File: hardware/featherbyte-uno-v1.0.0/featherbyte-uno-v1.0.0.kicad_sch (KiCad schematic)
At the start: 60 parts, among them J1 Conn_01x08, J10 Conn_01x09, J2 Conn_01x10, J3 Conn_01x06, J5 USB_C_Receptacle_16P, J6 SWD Connector, J7 Terminal Block, J8 USB_C_Receptacle_16P, J9 BOOT1, SW1 Reset, SW2 BOOT0, SW3 SW_DIP_x04, U1 CH32V203CxT6, U2 TJA1050, U4 AMS1117-3.3, U5 USBLC6-2P6, U6 USBLC6-2P6, Y1 8M, Y3 32.768K

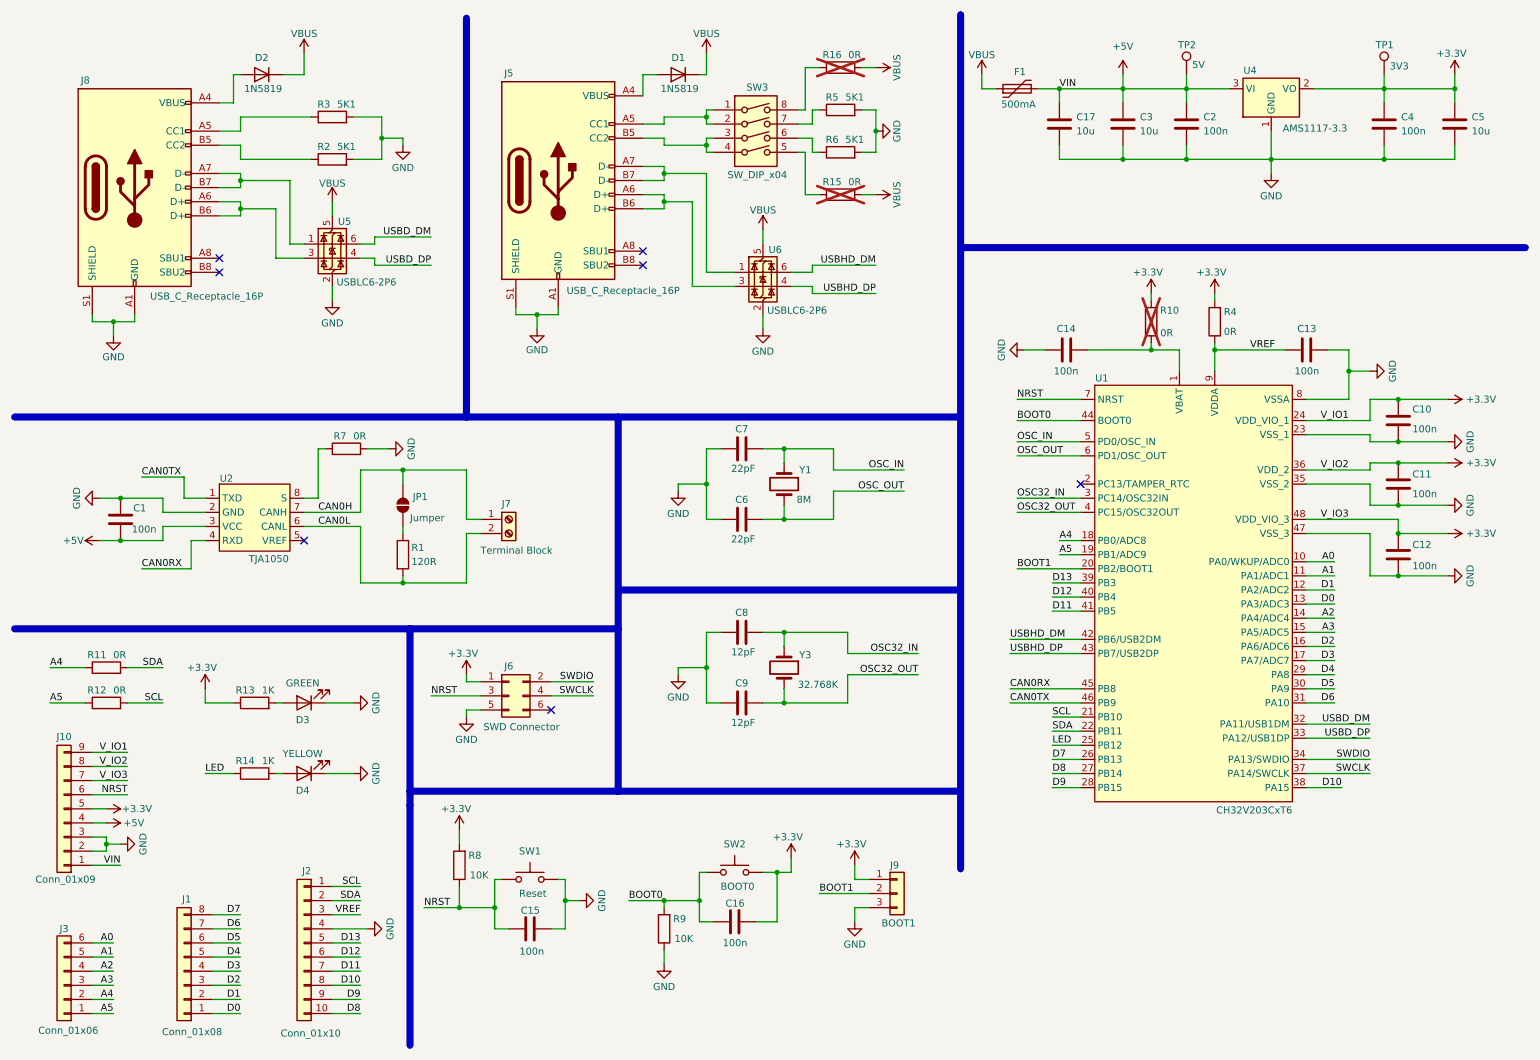
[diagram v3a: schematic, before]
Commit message: usb tvs diode orientation changed
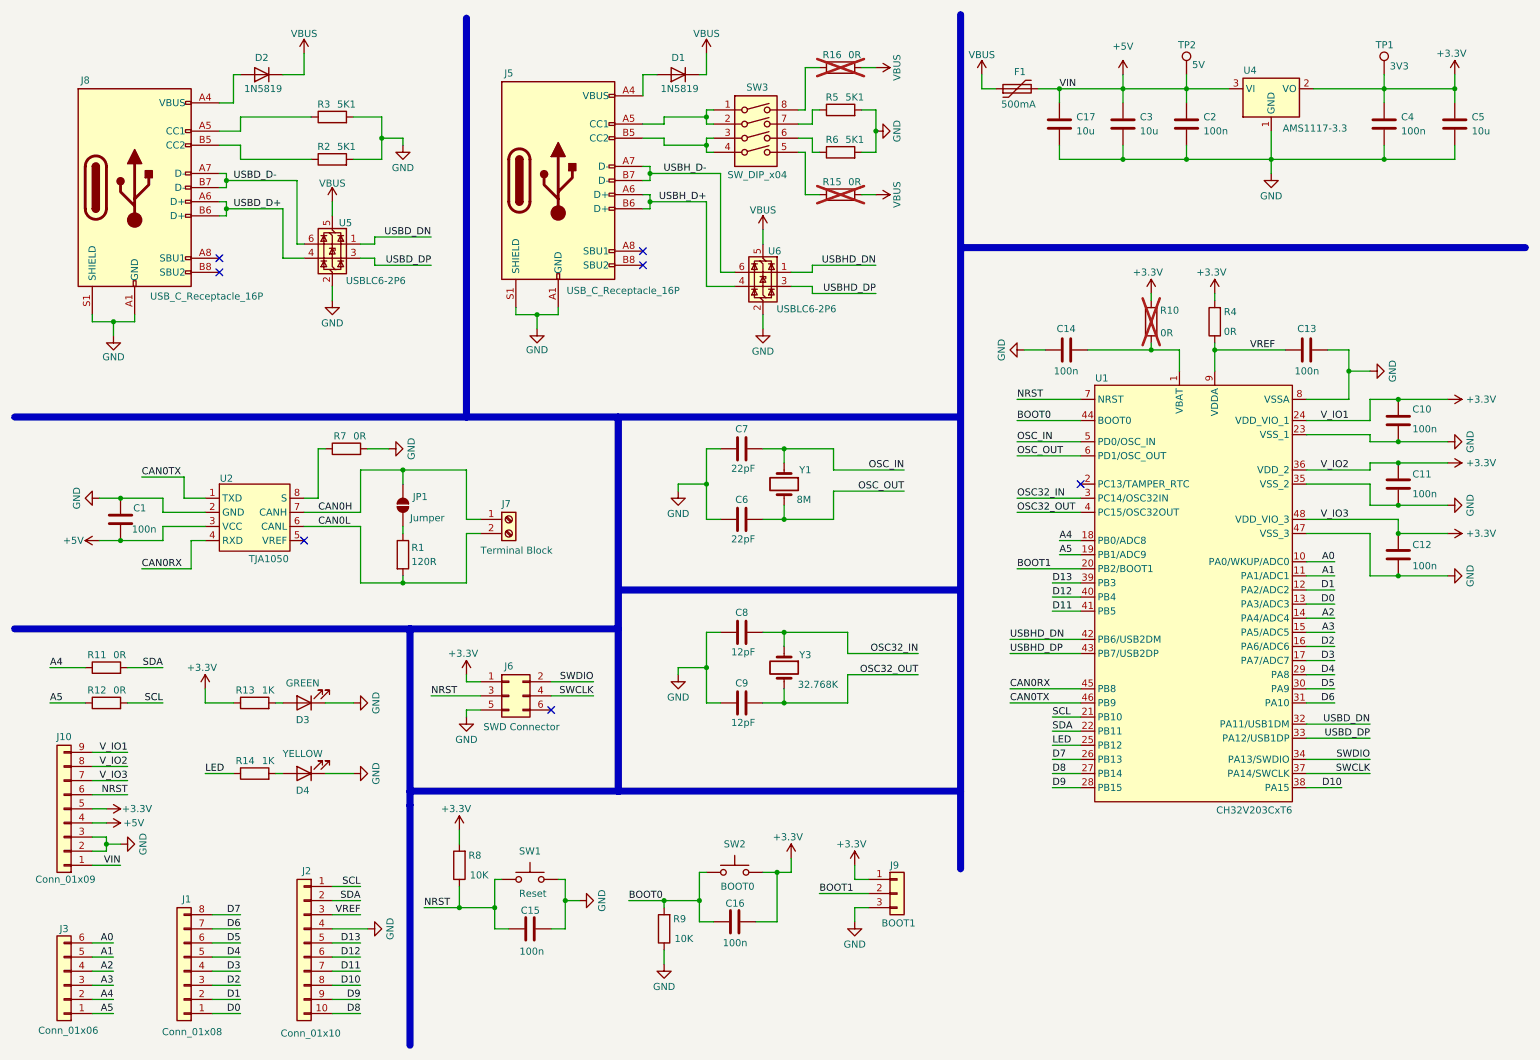
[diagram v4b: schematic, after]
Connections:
- net USBD_DP: now also U5.3 (I/O2); no longer U5.4 (I/O2)
- net USBHD_DP: now also U6.3 (I/O2); no longer U6.4 (I/O2)
- net USBD_D-: now reaches J8.A7 (D-), J8.B7 (D-)
- net USBD_D-: now also U5.6 (I/O1); no longer U5.1 (I/O1)
- net USBD_D+: now reaches J8.A6 (D+), J8.B6 (D+)
- net USBD_D+: now also U5.4 (I/O2); no longer U5.3 (I/O2)
- net USBH_D+: now reaches J5.A6 (D+), J5.B6 (D+)
- net USBH_D+: now also U6.4 (I/O2); no longer U6.3 (I/O2)
- net USBH_D-: now reaches J5.A7 (D-), J5.B7 (D-)
- net USBH_D-: now also U6.6 (I/O1); no longer U6.1 (I/O1)
- net USBD_DM renamed USBD_DN
- net USBD_DN: now also U5.1 (I/O1); no longer U5.6 (I/O1)
- net USBHD_DM renamed USBHD_DN
- net USBHD_DN: now also U6.1 (I/O1); no longer U6.6 (I/O1)

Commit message: can bus connector pins reversed
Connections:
- net CAN0H: now also J7.2 (Pin_2); no longer J7.1 (Pin_1)
- net CAN0L: now also J7.1 (Pin_1); no longer J7.2 (Pin_2)
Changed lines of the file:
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@@
 	(wire
 		(pts
+			(xy 93.98 105.41) (xy 96.52 105.41)
+		)
+		(stroke
+			(width 0)
+			(type default)
+		)
+	)
+	(wire
+		(pts
 			(xy 127 41.91) (xy 125.73 41.91)
 		)
@@
 	(wire
 		(pts
-			(xy 93.98 105.41) (xy 96.52 105.41)
-		)
-		(stroke
-			(width 0)
-			(type default)
-		)
-	)
-	(wire
-		(pts
 			(xy 162.56 135.89) (xy 162.56 130.81)
 		)
@@
 	(wire
 		(pts
-			(xy 93.98 102.87) (xy 96.52 102.87)
-		)
-		(stroke
-			(width 0)
-			(type default)
-		)
-	)
-	(wire
-		(pts
 			(xy 77.47 52.07) (xy 77.47 53.34)
 		)
@@
 	(wire
 		(pts
+			(xy 93.98 102.87) (xy 96.52 102.87)
+		)
+		(stroke
+			(width 0)
+			(type default)
+		)
+	)
+	(wire
+		(pts
 			(xy 129.54 35.56) (xy 129.54 34.29)
 		)
@@
 	(symbol
 		(lib_id "Connector:Screw_Terminal_01x02")
-		(at 101.6 102.87 0)
+		(at 101.6 105.41 0)
+		(mirror x)
 		(unit 1)
 		(exclude_from_sim no)
@@
 		(dnp no)
 		(property "Reference" "J7"
-			(at 100.33 100.076 0)
+			(at 100.838 100.584 0)
 			(effects
 				(font
@@
 		)
 		(property "Value" "Terminal Block"
-			(at 96.52 108.458 0)
+			(at 96.52 108.204 0)
 			(effects
 				(font
@@
 		)
 		(property "Footprint" "TerminalBlock:TerminalBlock_MaiXu_MX126-5.0-02P_1x02_P5.00mm"
-			(at 101.6 102.87 0)
+			(at 101.6 105.41 0)
 			(effects
 				(font
@@
 		)
 		(property "Datasheet" "~"
-			(at 101.6 102.87 0)
+			(at 101.6 105.41 0)
 			(effects
 				(font
@@
 		)
 		(property "Description" "Generic screw terminal, single row, 01x02, script generated (kicad-library-utils/schlib/autogen/connector/)"
-			(at 101.6 102.87 0)
+			(at 101.6 105.41 0)
 			(effects
 				(font

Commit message: pcb routing ongoing
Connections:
- net USBD_D+: now also U5.3 (I/O2); no longer U5.4 (I/O2)
- net USBD_D-: now also U5.1 (I/O1); no longer U5.6 (I/O1)
- net USBD_DN: now also U5.6 (I/O1); no longer U5.1 (I/O1)
- net USBD_DP: now also U5.4 (I/O2); no longer U5.3 (I/O2)
- net USBHD_DN: now also U6.6 (I/O1); no longer U6.1 (I/O1)
- net USBHD_DP: now also U6.4 (I/O2); no longer U6.3 (I/O2)
- net USBH_D+: now also U6.3 (I/O2); no longer U6.4 (I/O2)
- net USBH_D-: now also U6.1 (I/O1); no longer U6.6 (I/O1)
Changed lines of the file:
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@@
 	(wire
 		(pts
+			(xy 137.16 60.96) (xy 142.24 60.96)
+		)
+		(stroke
+			(width 0)
+			(type default)
+		)
+	)
+	(wire
+		(pts
 			(xy 245.11 85.09) (xy 256.54 85.09)
 		)
@@
 	(wire
 		(pts
+			(xy 139.7 58.42) (xy 142.24 58.42)
+		)
+		(stroke
+			(width 0)
+			(type default)
+		)
+	)
+	(wire
+		(pts
 			(xy 223.52 25.4) (xy 231.14 25.4)
 		)
@@
 	(wire
 		(pts
-			(xy 137.16 60.96) (xy 142.24 60.96)
-		)
-		(stroke
-			(width 0)
-			(type default)
-		)
-	)
-	(wire
-		(pts
 			(xy 250.19 133.35) (xy 245.11 133.35)
 		)
@@
 	(wire
 		(pts
-			(xy 152.4 60.96) (xy 156.21 60.96)
-		)
-		(stroke
-			(width 0)
-			(type default)
-		)
-	)
-	(wire
-		(pts
 			(xy 137.16 29.21) (xy 137.16 30.48)
 		)
@@
 	(wire
 		(pts
-			(xy 139.7 58.42) (xy 142.24 58.42)
-		)
-		(stroke
-			(width 0)
-			(type default)
-		)
-	)
-	(wire
-		(pts
 			(xy 250.19 128.27) (xy 245.11 128.27)
 		)
@@
 	(wire
 		(pts
+			(xy 74.93 55.88) (xy 77.47 55.88)
+		)
+		(stroke
+			(width 0)
+			(type default)
+		)
+	)
+	(wire
+		(pts
 			(xy 67.31 90.17) (xy 68.58 90.17)
 		)
@@
 	(wire
 		(pts
-			(xy 74.93 55.88) (xy 77.47 55.88)
-		)
-		(stroke
-			(width 0)
-			(type default)
-		)
-	)
-	(wire
-		(pts
 			(xy 26.67 162.56) (xy 29.21 162.56)
 		)
@@
 	(wire
 		(pts
-			(xy 74.93 114.3) (xy 82.55 114.3)
+			(xy 63.5 53.34) (xy 64.77 53.34)
 		)
 		(stroke
@@
 	(wire
 		(pts
-			(xy 152.4 58.42) (xy 156.21 58.42)
+			(xy 74.93 114.3) (xy 82.55 114.3)
 		)
 		(stroke
@@
 	(wire
 		(pts
-			(xy 60.96 55.88) (xy 64.77 55.88)
+			(xy 162.56 123.19) (xy 151.13 123.19)
 		)
 		(stroke
@@
 	(wire
 		(pts
-			(xy 162.56 123.19) (xy 151.13 123.19)
+			(xy 137.16 90.17) (xy 137.16 96.52)
 		)
 		(stroke
@@
 	(wire
 		(pts
-			(xy 137.16 90.17) (xy 137.16 96.52)
+			(xy 78.74 34.29) (xy 78.74 38.1)
 		)
 		(stroke
@@
 	(wire
 		(pts
-			(xy 78.74 34.29) (xy 78.74 38.1)
+			(xy 64.77 101.6) (xy 74.93 101.6)
 		)
 		(stroke
@@
 	(wire
 		(pts
-			(xy 64.77 101.6) (xy 74.93 101.6)
+			(xy 200.66 25.4) (xy 212.09 25.4)
 		)
 		(stroke
@@
 	(wire
 		(pts
-			(xy 200.66 25.4) (xy 212.09 25.4)
+			(xy 152.4 58.42) (xy 156.21 58.42)
 		)
 		(stroke
@@
 	(wire
 		(pts
+			(xy 60.96 55.88) (xy 64.77 55.88)
+		)
+		(stroke
+			(width 0)
+			(type default)
+		)
+	)
+	(wire
+		(pts
 			(xy 50.8 40.64) (xy 50.8 41.91)
 		)
@@
 	(wire
 		(pts
-			(xy 63.5 53.34) (xy 64.77 53.34)
-		)
-		(stroke
-			(width 0)
-			(type default)
-		)
-	)
-	(wire
-		(pts
 			(xy 250.19 125.73) (xy 245.11 125.73)
 		)
@@
 	(wire
 		(pts
+			(xy 74.93 53.34) (xy 77.47 53.34)
+		)
+		(stroke
+			(width 0)
+			(type default)
+		)
+	)
+	(wire
+		(pts
 			(xy 186.69 25.4) (xy 189.23 25.4)
 		)
@@
 	(wire
 		(pts
-			(xy 74.93 53.34) (xy 77.47 53.34)
-		)
-		(stroke
-			(width 0)
-			(type default)
-		)
-	)
-	(wire
-		(pts
 			(xy 93.98 137.16) (xy 93.98 138.43)
 		)
@@
 	(wire
 		(pts
+			(xy 152.4 60.96) (xy 156.21 60.96)
+		)
+		(stroke
+			(width 0)
+			(type default)
+		)
+	)
+	(wire
+		(pts
 			(xy 46.99 133.35) (xy 46.99 135.89)
 		)
@@
 		(lib_id "Power_Protection:USBLC6-2P6")
 		(at 69.85 53.34 0)
-		(mirror y)
 		(unit 1)
 		(exclude_from_sim no)
@@
 		(dnp no)
 		(property "Reference" "U5"
-			(at 73.406 49.53 0)
+			(at 71.12 49.276 0)
 			(effects
 				(font
@@
 		)
 		(property "Value" "USBLC6-2P6"
-			(at 83.058 59.944 0)
+			(at 70.358 59.944 0)
 			(effects
 				(font
@@
 		)
 		(property "Footprint" "Package_TO_SOT_SMD:SOT-666"
-			(at 68.834 60.071 0)
+			(at 70.866 60.071 0)
 			(effects
 				(font
@@
 		)
 		(property "Datasheet" "https://www.st.com/resource/en/datasheet/usblc6-2.pdf"
-			(at 68.834 61.976 0)
+			(at 70.866 61.976 0)
 			(effects
 				(font
@@
 		(lib_id "Power_Protection:USBLC6-2P6")
 		(at 147.32 58.42 0)
-		(mirror y)
 		(unit 1)
 		(exclude_from_sim no)
@@
 		(dnp no)
 		(property "Reference" "U6"
-			(at 150.622 54.61 0)
+			(at 148.336 54.356 0)
 			(effects
 				(font
@@
 		)
 		(property "Value" "USBLC6-2P6"
-			(at 160.528 65.024 0)
+			(at 148.336 65.024 0)
 			(effects
 				(font
@@
 		)
 		(property "Footprint" "Package_TO_SOT_SMD:SOT-666"
-			(at 146.304 65.151 0)
+			(at 148.336 65.151 0)
 			(effects
 				(font
@@
 		)
 		(property "Datasheet" "https://www.st.com/resource/en/datasheet/usblc6-2.pdf"
-			(at 146.304 67.056 0)
+			(at 148.336 67.056 0)
 			(effects
 				(font

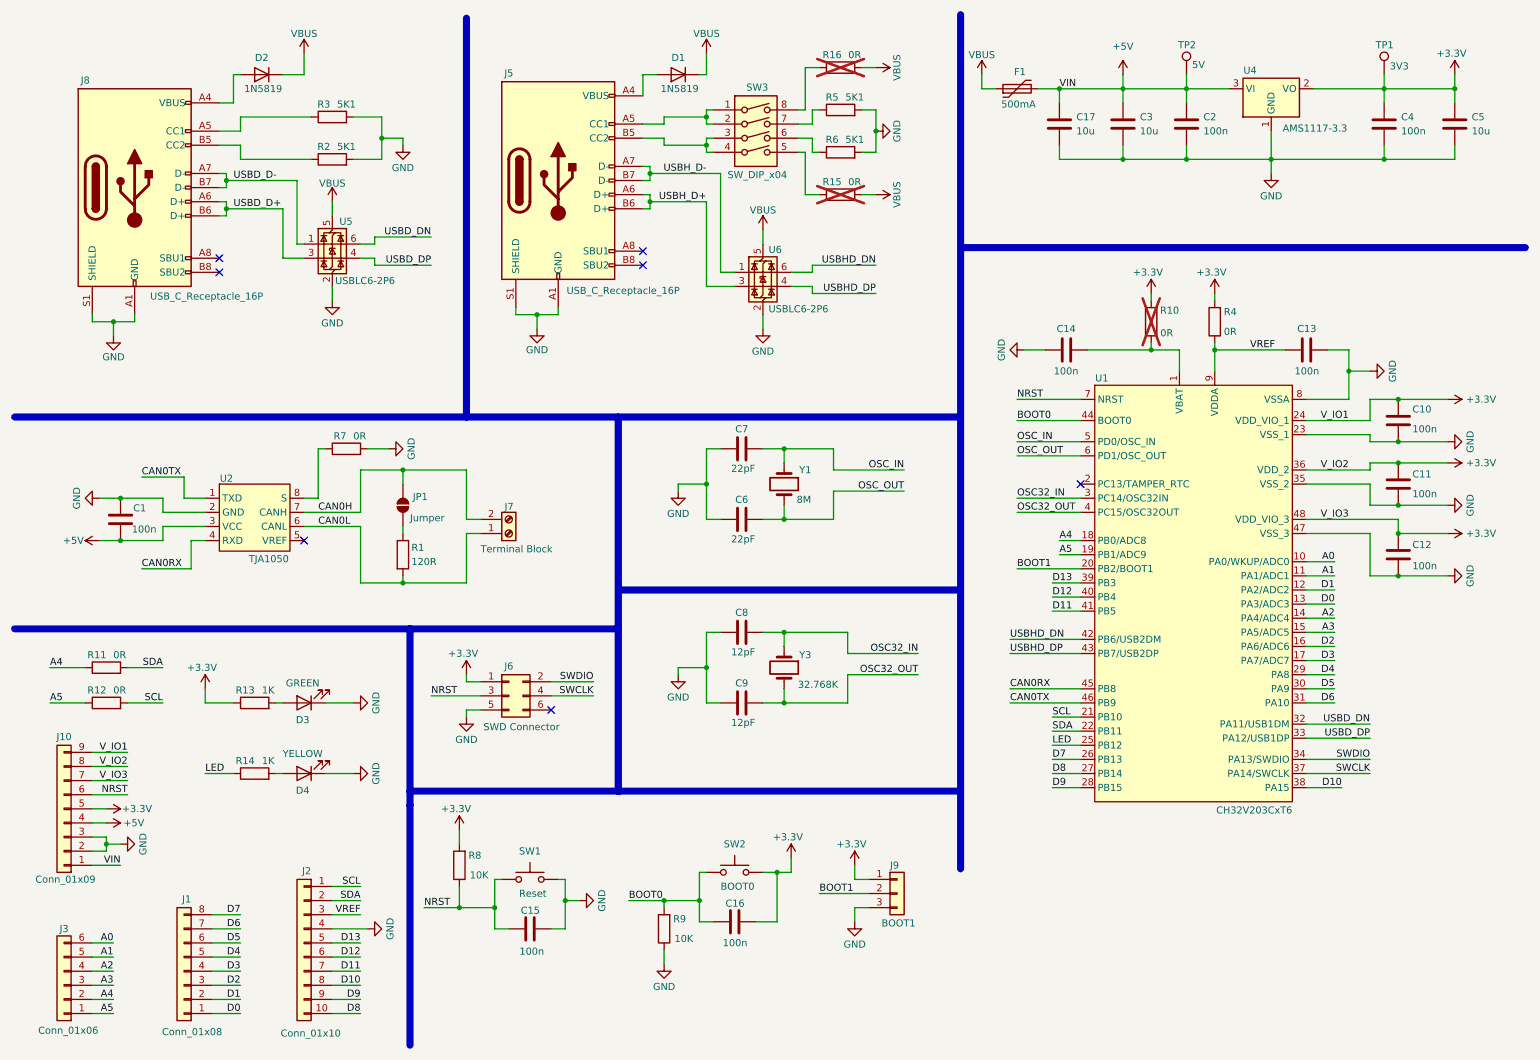
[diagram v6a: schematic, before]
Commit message: restarted routing and positioning process
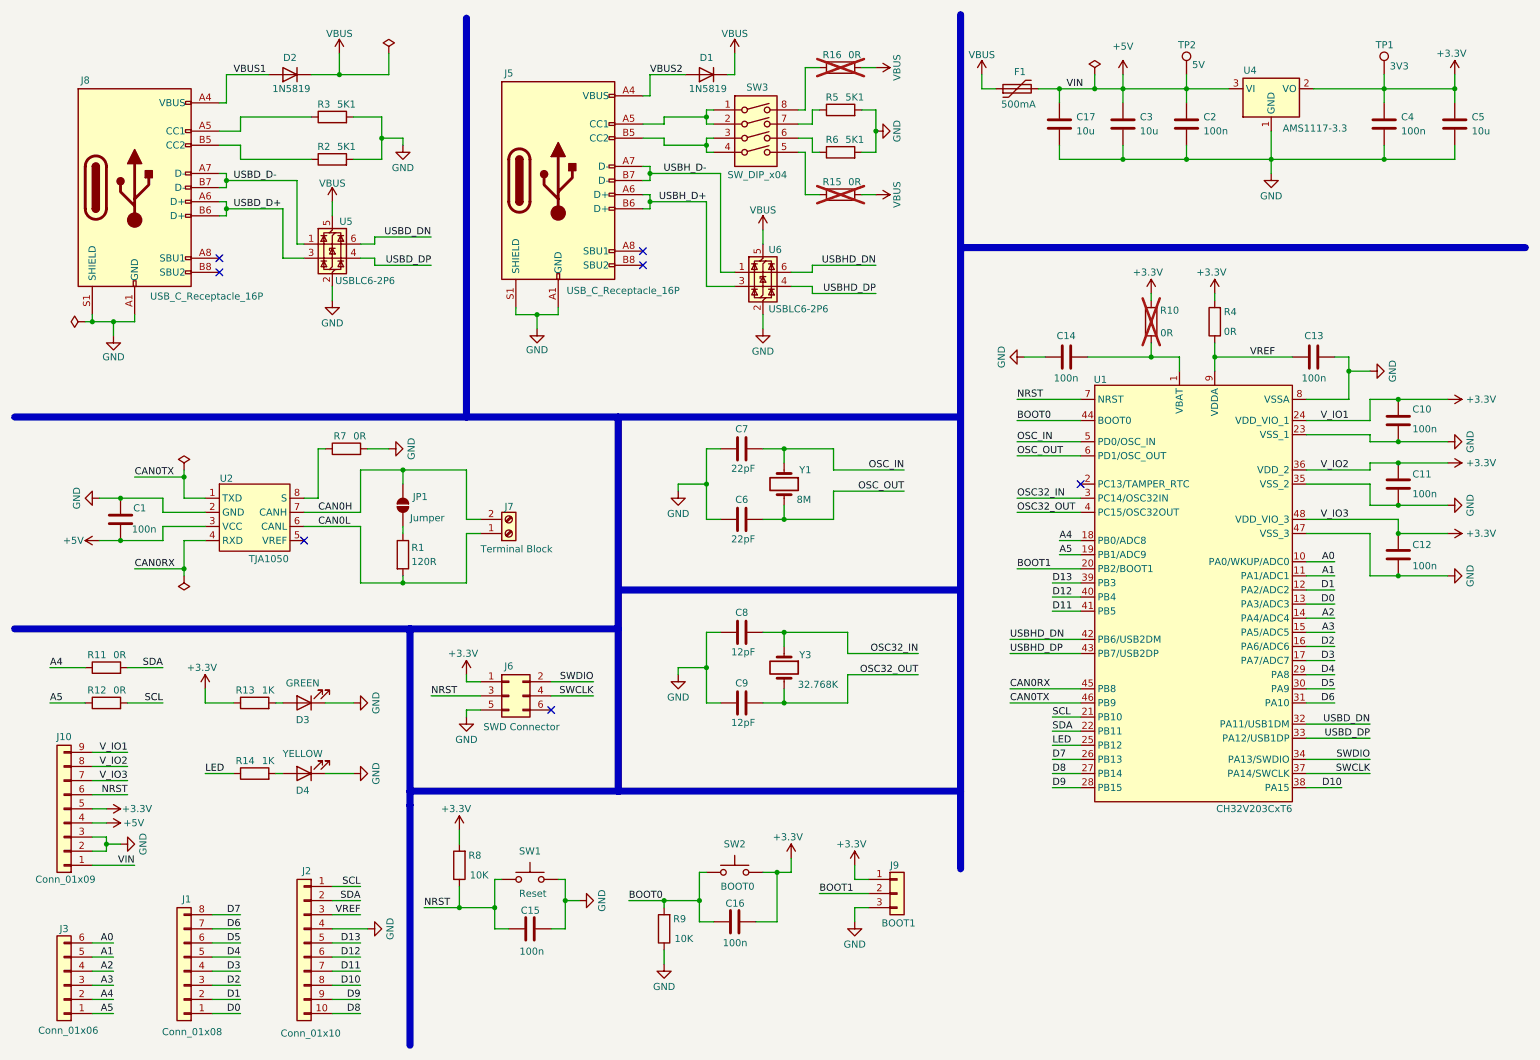
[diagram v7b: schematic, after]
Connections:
- net VBUS1: now reaches D2.2 (A), J8.A4 (VBUS), J8.A9 (VBUS), J8.B4 (VBUS), J8.B9 (VBUS)
- net VBUS2: now reaches D1.2 (A), J5.A4 (VBUS), J5.A9 (VBUS), J5.B4 (VBUS), J5.B9 (VBUS)
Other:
- moved on the sheet: C13, C14, D1, D2
